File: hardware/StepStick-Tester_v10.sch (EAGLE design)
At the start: 10 parts, among them IC1 STEPSTICK-TP, J1 MA08-1, J2 MA08-1, J3 MA04-1

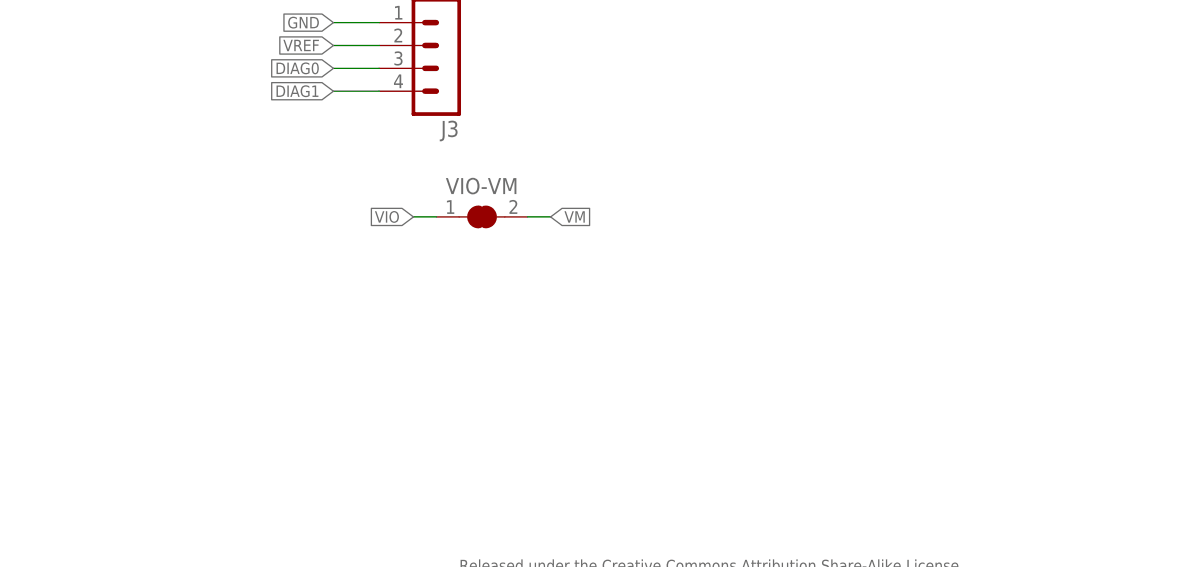
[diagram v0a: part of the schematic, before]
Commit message: updated schematics
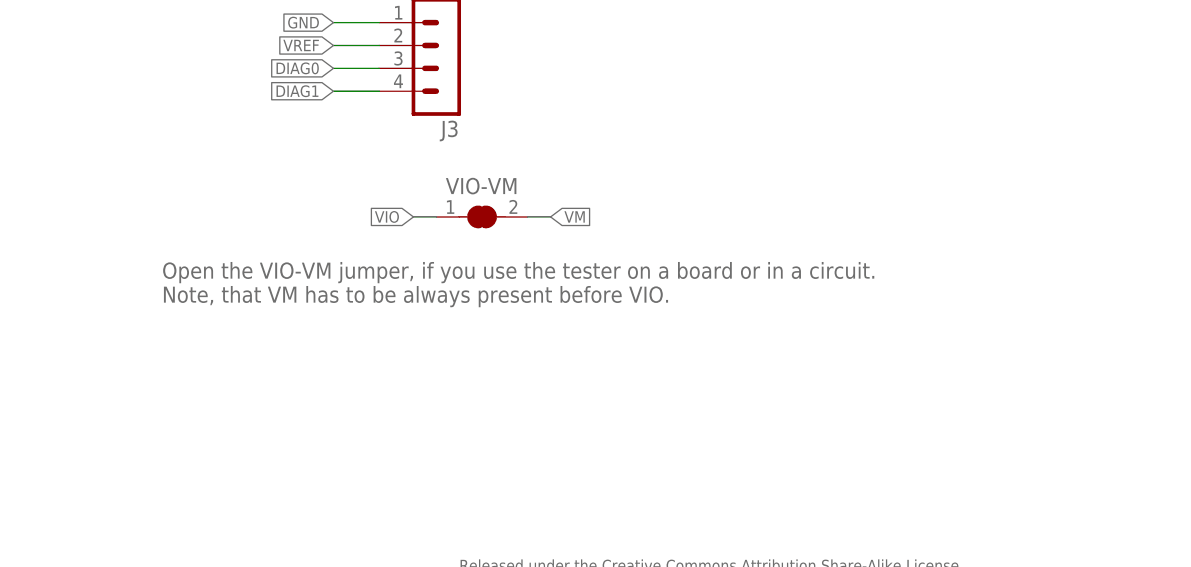
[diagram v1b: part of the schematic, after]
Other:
- note added: "Open the VIO-VM jumper, if you use the tester on a board or in a circuit. Note, that VM has to be always present before VIO."
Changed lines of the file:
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@@
 <setting verticaltext="up"/>
 </settings>
-<grid distance="0.05" unitdist="inch" unit="inch" style="lines" multiple="1" display="yes" altdistance="0.025" altunitdist="inch" altunit="inch"/>
+<grid distance="0.1" unitdist="inch" unit="inch" style="lines" multiple="1" display="no" altdistance="0.01" altunitdist="inch" altunit="inch"/>
 <layers>
-<layer number="1" name="Top" color="4" fill="1" visible="yes" active="no"/>
-<layer number="2" name="Route2" color="1" fill="3" visible="yes" active="no"/>
-<layer number="3" name="Route3" color="4" fill="3" visible="yes" active="no"/>
-<layer number="4" name="Route4" color="1" fill="4" visible="yes" active="no"/>
-<layer number="5" name="Route5" color="4" fill="4" visible="yes" active="no"/>
-<layer number="6" name="Route6" color="1" fill="8" visible="yes" active="no"/>
-<layer number="7" name="Route7" color="4" fill="8" visible="yes" active="no"/>
-<layer number="8" name="Route8" color="1" fill="2" visible="yes" active="no"/>
-<layer number="9" name="Route9" color="4" fill="2" visible="yes" active="no"/>
-<layer number="10" name="Route10" color="1" fill="7" visible="yes" active="no"/>
-<layer number="11" name="Route11" color="4" fill="7" visible="yes" active="no"/>
-<layer number="12" name="Route12" color="1" fill="5" visible="yes" active="no"/>
-<layer number="13" name="Route13" color="4" fill="5" visible="yes" active="no"/>
-<layer number="14" name="Route14" color="1" fill="6" visible="yes" active="no"/>
-<layer number="15" name="Route15" color="4" fill="6" visible="yes" active="no"/>
-<layer number="16" name="Bottom" color="1" fill="1" visible="yes" active="no"/>
-<layer number="17" name="Pads" color="2" fill="1" visible="yes" active="no"/>
-<layer number="18" name="Vias" color="2" fill="1" visible="yes" active="no"/>
-<layer number="19" name="Unrouted" color="6" fill="1" visible="yes" active="no"/>
-<layer number="20" name="Dimension" color="15" fill="1" visible="yes" active="no"/>
-<layer number="21" name="tPlace" color="7" fill="1" visible="yes" active="no"/>
-<layer number="22" name="bPlace" color="7" fill="1" visible="yes" active="no"/>
-<layer number="23" name="tOrigins" color="15" fill="1" visible="yes" active="no"/>
-<layer number="24" name="bOrigins" color="15" fill="1" visible="yes" active="no"/>
-<layer number="25" name="tNames" color="7" fill="1" visible="yes" active="no"/>
-<layer number="26" name="bNames" color="7" fill="1" visible="yes" active="no"/>
-<layer number="27" name="tValues" color="7" fill="1" visible="yes" active="no"/>
-<layer number="28" name="bValues" color="7" fill="1" visible="yes" active="no"/>
+<layer number="1" name="Top" color="4" fill="1" visible="no" active="no"/>
+<layer number="2" name="Route2" color="1" fill="3" visible="no" active="no"/>
+<layer number="3" name="Route3" color="4" fill="3" visible="no" active="no"/>
+<layer number="4" name="Route4" color="1" fill="4" visible="no" active="no"/>
+<layer number="5" name="Route5" color="4" fill="4" visible="no" active="no"/>
+<layer number="6" name="Route6" color="1" fill="8" visible="no" active="no"/>
+<layer number="7" name="Route7" color="4" fill="8" visible="no" active="no"/>
+<layer number="8" name="Route8" color="1" fill="2" visible="no" active="no"/>
+<layer number="9" name="Route9" color="4" fill="2" visible="no" active="no"/>
+<layer number="10" name="Route10" color="1" fill="7" visible="no" active="no"/>
+<layer number="11" name="Route11" color="4" fill="7" visible="no" active="no"/>
+<layer number="12" name="Route12" color="1" fill="5" visible="no" active="no"/>
+<layer number="13" name="Route13" color="4" fill="5" visible="no" active="no"/>
+<layer number="14" name="Route14" color="1" fill="6" visible="no" active="no"/>
+<layer number="15" name="Route15" color="4" fill="6" visible="no" active="no"/>
+<layer number="16" name="Bottom" color="1" fill="1" visible="no" active="no"/>
+<layer number="17" name="Pads" color="2" fill="1" visible="no" active="no"/>
+<layer number="18" name="Vias" color="2" fill="1" visible="no" active="no"/>
+<layer number="19" name="Unrouted" color="6" fill="1" visible="no" active="no"/>
+<layer number="20" name="Dimension" color="15" fill="1" visible="no" active="no"/>
+<layer number="21" name="tPlace" color="7" fill="1" visible="no" active="no"/>
+<layer number="22" name="bPlace" color="7" fill="1" visible="no" active="no"/>
+<layer number="23" name="tOrigins" color="15" fill="1" visible="no" active="no"/>
+<layer number="24" name="bOrigins" color="15" fill="1" visible="no" active="no"/>
+<layer number="25" name="tNames" color="7" fill="1" visible="no" active="no"/>
+<layer number="26" name="bNames" color="7" fill="1" visible="no" active="no"/>
+<layer number="27" name="tValues" color="7" fill="1" visible="no" active="no"/>
+<layer number="28" name="bValues" color="7" fill="1" visible="no" active="no"/>
 <layer number="29" name="tStop" color="7" fill="3" visible="no" active="no"/>
 <layer number="30" name="bStop" color="7" fill="6" visible="no" active="no"/>
@@
 <layer number="35" name="tGlue" color="7" fill="4" visible="no" active="no"/>
 <layer number="36" name="bGlue" color="7" fill="5" visible="no" active="no"/>
-<layer number="37" name="tTest" color="7" fill="1" visible="yes" active="no"/>
-<layer number="38" name="bTest" color="7" fill="1" visible="yes" active="no"/>
+<layer number="37" name="tTest" color="7" fill="1" visible="no" active="no"/>
+<layer number="38" name="bTest" color="7" fill="1" visible="no" active="no"/>
 <layer number="39" name="tKeepout" color="4" fill="11" visible="no" active="no"/>
 <layer number="40" name="bKeepout" color="1" fill="11" visible="no" active="no"/>
@@
 <layer number="44" name="Drills" color="7" fill="1" visible="no" active="no"/>
 <layer number="45" name="Holes" color="7" fill="1" visible="no" active="no"/>
-<layer number="46" name="Milling" color="3" fill="1" visible="yes" active="no"/>
-<layer number="47" name="Measures" color="7" fill="1" visible="yes" active="no"/>
-<layer number="48" name="Document" color="7" fill="1" visible="yes" active="no"/>
-<layer number="49" name="Reference" color="7" fill="1" visible="yes" active="no"/>
-<layer number="50" name="dxf" color="7" fill="1" visible="yes" active="no"/>
-<layer number="51" name="tDocu" color="7" fill="1" visible="yes" active="no"/>
-<layer number="52" name="bDocu" color="7" fill="1" visible="yes" active="no"/>
+<layer number="46" name="Milling" color="3" fill="1" visible="no" active="no"/>
+<layer number="47" name="Measures" color="7" fill="1" visible="no" active="no"/>
+<layer number="48" name="Document" color="7" fill="1" visible="no" active="no"/>
+<layer number="49" name="Reference" color="7" fill="1" visible="no" active="no"/>
+<layer number="50" name="dxf" color="7" fill="1" visible="no" active="no"/>
+<layer number="51" name="tDocu" color="7" fill="1" visible="no" active="no"/>
+<layer number="52" name="bDocu" color="7" fill="1" visible="no" active="no"/>
 <layer number="90" name="Modules" color="5" fill="1" visible="yes" active="yes"/>
 <layer number="91" name="Nets" color="2" fill="1" visible="yes" active="yes"/>
@@
 <text x="162.56" y="15.24" size="1.27" layer="95">Designed by Andreas Watterott (Watterott electronic)</text>
 <wire x1="164.465" y1="60.96" x2="165.735" y2="60.96" width="0.4064" layer="94"/>
+<text x="129.54" y="55.88" size="1.778" layer="95" font="vector" ratio="10" align="top-left">Open the VIO-VM jumper, if you use the tester on a board or in a circuit.
+Note, that VM has to be always present before VIO.</text>
 </plain>
 <instances>
@@
 </schematic>
 </drawing>
+<compatibility>
+<note version="6.3" minversion="6.2.2" severity="warning">
+Since Version 6.2.2 text objects can contain more than one line,
+which will not be processed correctly with this version.
+</note>
+</compatibility>
 </eagle>
